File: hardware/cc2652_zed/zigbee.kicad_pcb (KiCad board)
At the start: 4 copper layers, 26.3 x 25.1 mm, 31 parts, among them J1 Conn_02x05_Odd_Even, J2 Conn_01x04, J3 Conn_01x04, SW1 EVQ-P7A01P-switch2, SW2 EVQ-P7A01P-switch2, U2 CC2652R1FRGZR, Y1 Crystal_GND24, Y2 Crystal

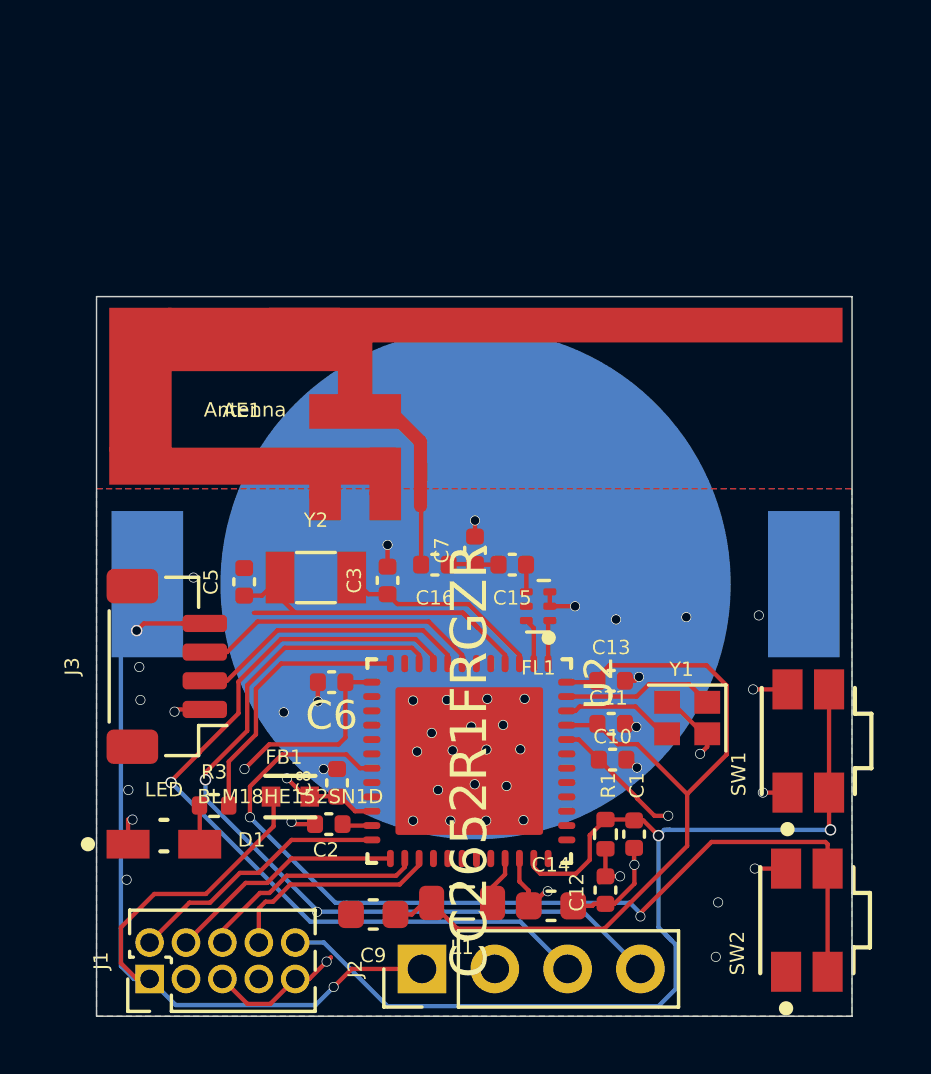
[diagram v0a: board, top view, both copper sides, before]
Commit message: update pcb of zed add devices.js mods for zigbee2mqtt
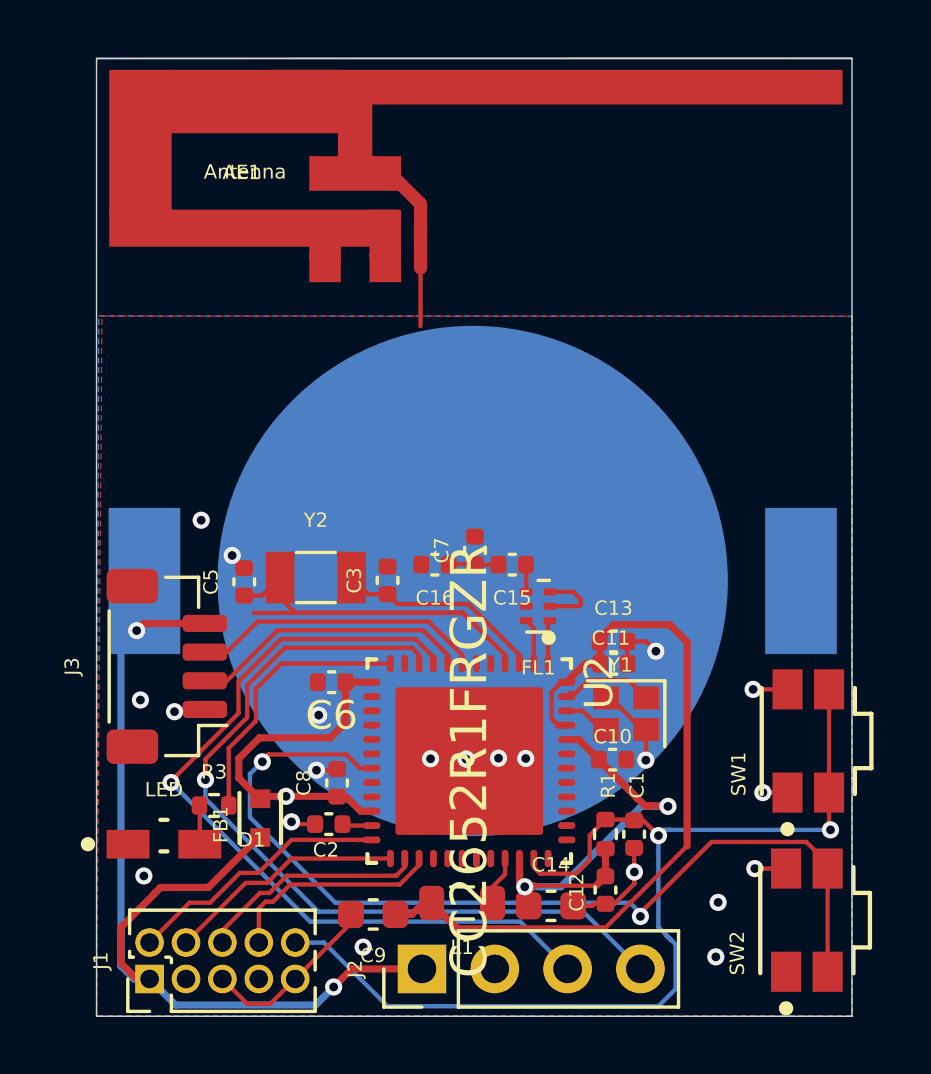
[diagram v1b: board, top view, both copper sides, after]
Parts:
- moved AE1 8.30 mm to (151.2, 107.6)
- moved Y1 2.14 mm to (158.4, 123.2)
- moved C11 2.09 mm to (157.9, 121.4)
- moved C13 1.37 mm to (157.9, 120.6)
- moved FB1 1.29 mm to (145.6, 126.8), turned to 90 degrees
- moved BT1 0.15 mm to (153.0, 118.5)
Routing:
- net VDDS: track 20.7 -> 32.6 mm, vias 5 -> 3
- net VDDR: track 29.5 -> 27.1 mm
- net Net-(U2-Pad46): track 3.96 -> 1.64 mm
- net Net-(U2-Pad47): track 5.34 -> 3.27 mm
- net VDD: track 37.1 -> 35.3 mm
- net Net-(AE1-Pad1): track 2.06 -> 2.81 mm
- net GND: track 22.9 -> 23.2 mm, vias 38 -> 21
- net /SDA: vias 2 -> 1
- net (no net): vias 8 -> 0
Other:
- board size 26.3 x 25.1 mm -> 26.3 x 33.4 mm
- net class Default: via_dia 0.35 -> 0.6; via_drill 0.3 -> 0.3048
- net class power added: clearance 0.1524, trace_width 0.25, via_dia 0.6, via_drill 0.3048
- rule trace_min: 0.1524 -> 0.15
- rule via_min_drill: 0.3 -> 0.3048
- rule via_min_size: 0.3 -> 0.6
